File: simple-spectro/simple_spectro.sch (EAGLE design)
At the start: 54 parts, among them IC1 MCP1703-33, IC2 MCP1703-50, J2 RJ12RIGHTANGLE-I2C, Q1 DMP1045U, U1 MCP73831T-2ACI/OT, X2 8MHz, X4 MINI-USB

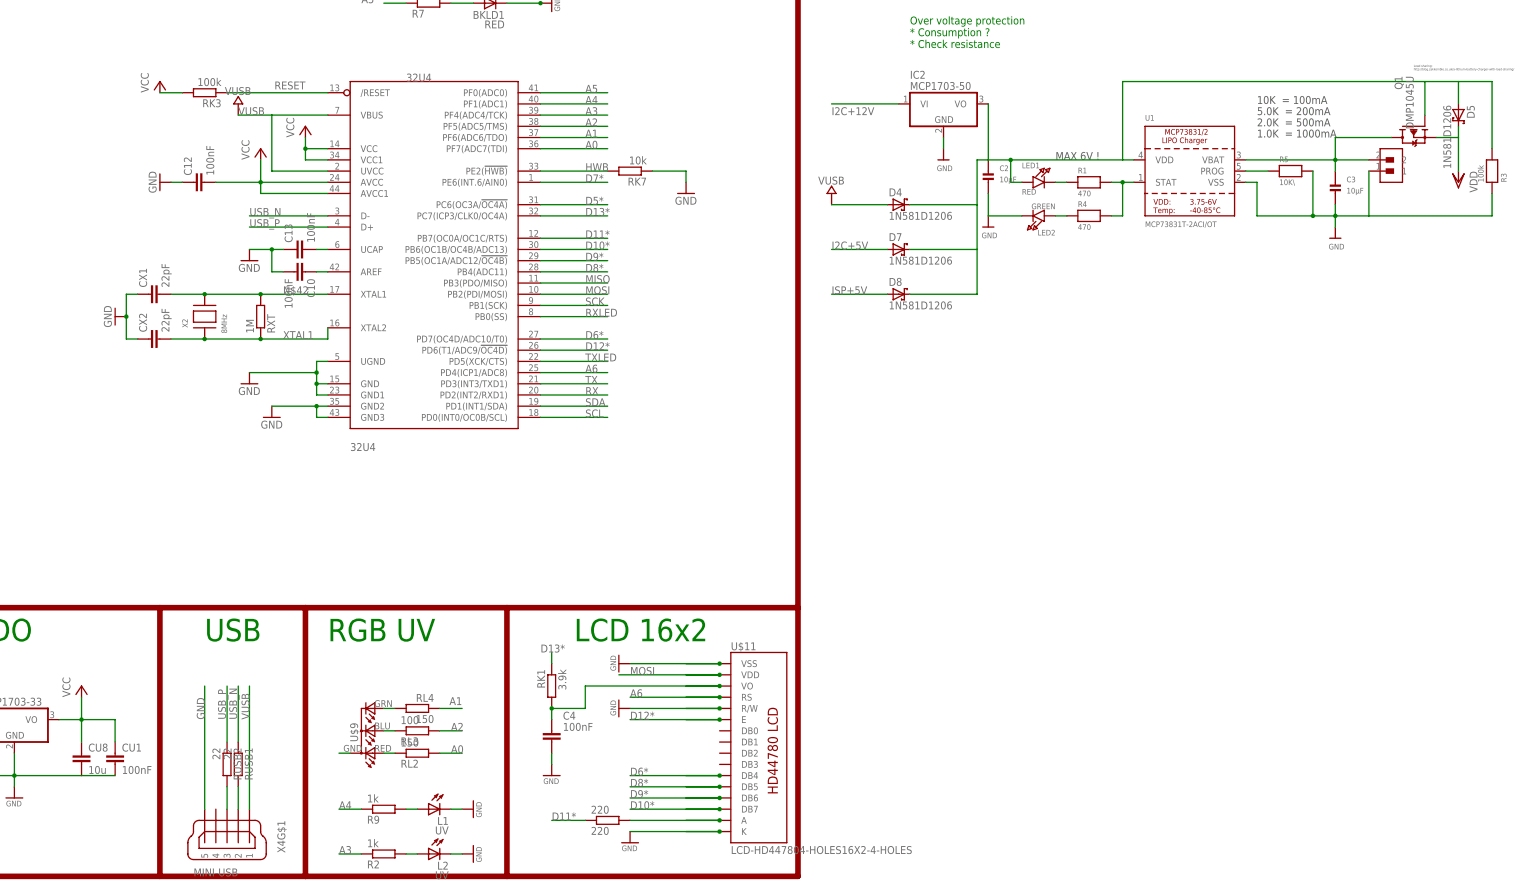
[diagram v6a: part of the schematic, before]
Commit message: first version of simple spectro
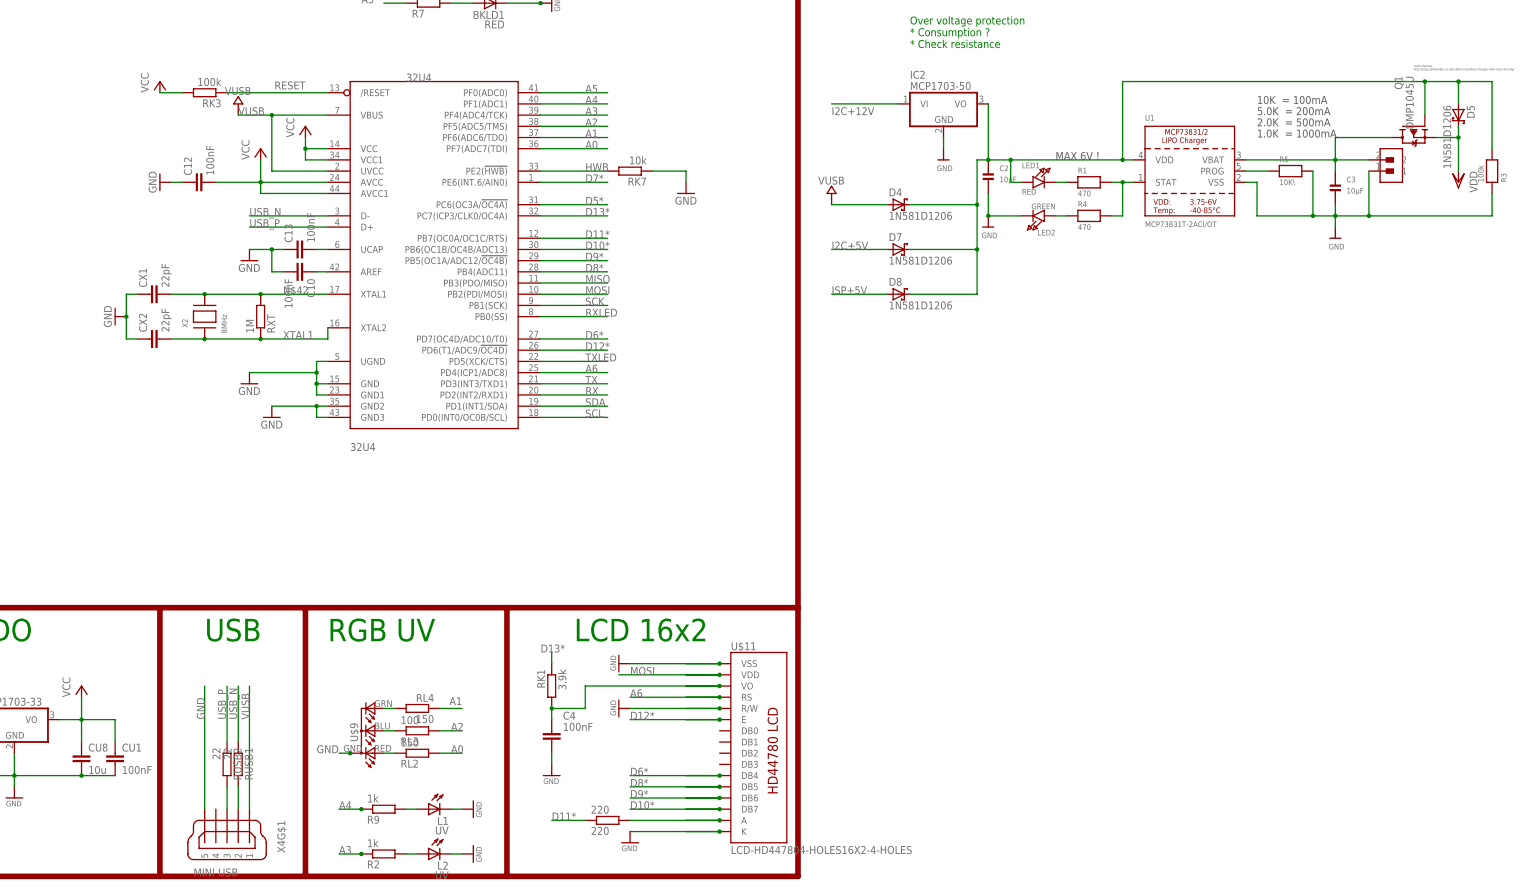
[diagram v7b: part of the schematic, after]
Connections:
- removed net GND1: U$9.A2
- net GND: now also U$9.A2
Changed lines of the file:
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@@
 <wire x1="350.52" y1="162.56" x2="350.52" y2="157.48" width="0.1524" layer="91"/>
 <pinref part="U$12" gate="G$1" pin="1"/>
+<junction x="322.58" y="157.48"/>
 </segment>
 <segment>
@@
 <wire x1="236.22" y1="162.56" x2="236.22" y2="157.48" width="0.1524" layer="91"/>
 <wire x1="243.84" y1="157.48" x2="236.22" y2="157.48" width="0.1524" layer="91"/>
+<junction x="236.22" y="157.48"/>
 </segment>
 <segment>
@@
 <pinref part="CU1" gate="G$1" pin="2"/>
 <wire x1="30.48" y1="30.48" x2="38.1" y2="30.48" width="0.1524" layer="91"/>
+<junction x="30.48" y="30.48"/>
 </segment>
 <segment>
@@
 <pinref part="L2" gate="G$1" pin="C"/>
 <wire x1="116.84" y1="12.7" x2="114.3" y2="12.7" width="0.1524" layer="91"/>
+</segment>
+<segment>
+<pinref part="U$9" gate="G$1" pin="A2"/>
+<wire x1="91.44" y1="35.56" x2="88.9" y2="35.56" width="0.1524" layer="91"/>
+<junction x="91.44" y="35.56"/>
+<label x="83.82" y="35.56" size="1.778" layer="95"/>
 </segment>
 </net>
@@
 <wire x1="93.98" y1="12.7" x2="88.9" y2="12.7" width="0.1524" layer="91"/>
 <label x="88.9" y="12.7" size="1.778" layer="95"/>
+<junction x="93.98" y="12.7"/>
 </segment>
 </net>
@@
 <wire x1="93.98" y1="22.86" x2="88.9" y2="22.86" width="0.1524" layer="91"/>
 <label x="88.9" y="22.86" size="1.778" layer="95"/>
+<junction x="93.98" y="22.86"/>
 </segment>
 </net>
@@
 <wire x1="86.36" y1="167.64" x2="73.66" y2="167.64" width="0.1524" layer="91"/>
 <wire x1="73.66" y1="167.64" x2="73.66" y2="180.34" width="0.1524" layer="91"/>
+<junction x="73.66" y="180.34"/>
 </segment>
 <segment>
@@
 </segment>
 </net>
-<net name="GND1" class="1">
-<segment>
-<pinref part="U$9" gate="G$1" pin="A2"/>
-<wire x1="91.44" y1="35.56" x2="88.9" y2="35.56" width="0.1524" layer="91"/>
-</segment>
-</net>
 <net name="N$9" class="0">
 <segment>
@@
 <wire x1="342.9" y1="175.26" x2="342.9" y2="177.8" width="0.1524" layer="91"/>
 <pinref part="SUPPLY4" gate="G$1" pin="VDD"/>
+<junction x="342.9" y="175.26"/>
 </segment>
 </net>
@@
 <pinref part="IC2" gate="G$1" pin="VO"/>
 <wire x1="236.22" y1="182.88" x2="236.22" y2="170.18" width="0.1524" layer="91"/>
-</segment>
-</net>
+<junction x="266.7" y="170.18"/>
+<junction x="233.68" y="149.86"/>
+<junction x="233.68" y="160.02"/>
+<junction x="342.9" y="187.96"/>
+<junction x="335.28" y="187.96"/>
+<junction x="236.22" y="170.18"/>
+</segment>
+</net>

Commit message: Update
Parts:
- removed C3: 10µF, microbuilder:CAP_CERAMIC0805
- removed D5: 1N581D1206, lpatiny:1N581D1206
- removed L1: UV, SparkFun:LED5MM
- removed L2: UV, led:LED3MM
- removed LED1: RED, microbuilder:LED0805
- removed LED2: GREEN, microbuilder:LED0805
- removed Q1: DMP1045U, dp_devices:TRANSISTOR_FET_TSM2301CX
- removed R1, R4: 470, microbuilder:RESISTOR0805
- removed R2, R9: 1k, rcl:R-EU_R0805
- removed R3: 100k, microbuilder:RESISTOR0805
- removed R5: 10K\, microbuilder:RESISTOR0805
- removed RL2, RL4: 150, rcl:R-EU_R0805
- removed RL3: 100, rcl:R-EU_R0805
- removed U$12: CONN2, lpatiny:CONN2
- removed U$7: TSL237, lpatiny:TSL237
- removed U$9: RGB-COMMON-CATHODE, lpatiny:RGB-COMMON-CATHODE
- removed U1: MCP73831T-2ACI/OT, microbuilder:MCP73831/2
- IC1: value MCP1703-33 -> MCP1703-50
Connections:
- removed net N$10: RL3.1, U$9.CBLUE
- removed net N$13: RL2.1, U$9.CRED
- removed net N$15: C2.P$1, D4.C, D5.A, D7.C, D8.C, IC2.VO, LED1.A, Q1.G, R3.2, U1.VDD
- removed net N$3: L1.A, R9.2
- removed net N$4: LED1.C, R1.1
- removed net N$5: R1.2, R4.2, U1.STAT
- removed net N$6: R5.1, U1.PROG
- removed net N$7: LED2.A, R4.1
- removed net N$8: L2.A, R2.2
- removed net N$9: RL4.2, U$9.CGREEN
- removed net VBAT1: C3.P$1, Q1.D, U$12.2, U1.VBAT
- new net N$19: C2.P$1, D4.C, D7.C, D8.C, IC2.VO
- net A0: no longer RL2.2
- net A1: no longer RL4.1
- net A2: no longer RL3.2
- net A3: no longer R2.1
- net A4: no longer R9.1
- net D5*: no longer U$7.OUT
- net GND: no longer C3.P$2, L1.C, L2.C, LED2.C, R3.1, R5.2, U$12.1, U$7.GND, U$9.A2, U1.VSS
- net VCC: no longer U$7.VDD
- net VDD: no longer D5.C, Q1.S
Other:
- note added: "5.0V LDO"
- note removed: "1.0K = 1000mA"
- note removed: "10K = 100mA"
- note removed: "2.0K = 500mA"
- note removed: "3.3V LDO"
- note removed: "5.0K = 200mA"
- note removed: "Load sharing: http://blog.zakkemble.co.uk/a-lithium-battery-charger-with-load-sharing/"
- note removed: "MAX 6V !"
- note removed: "Over voltage protection * Consumption ? * Check resistance"
